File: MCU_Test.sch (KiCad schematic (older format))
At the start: 18 parts, among them U2 STM32F051K6Ux

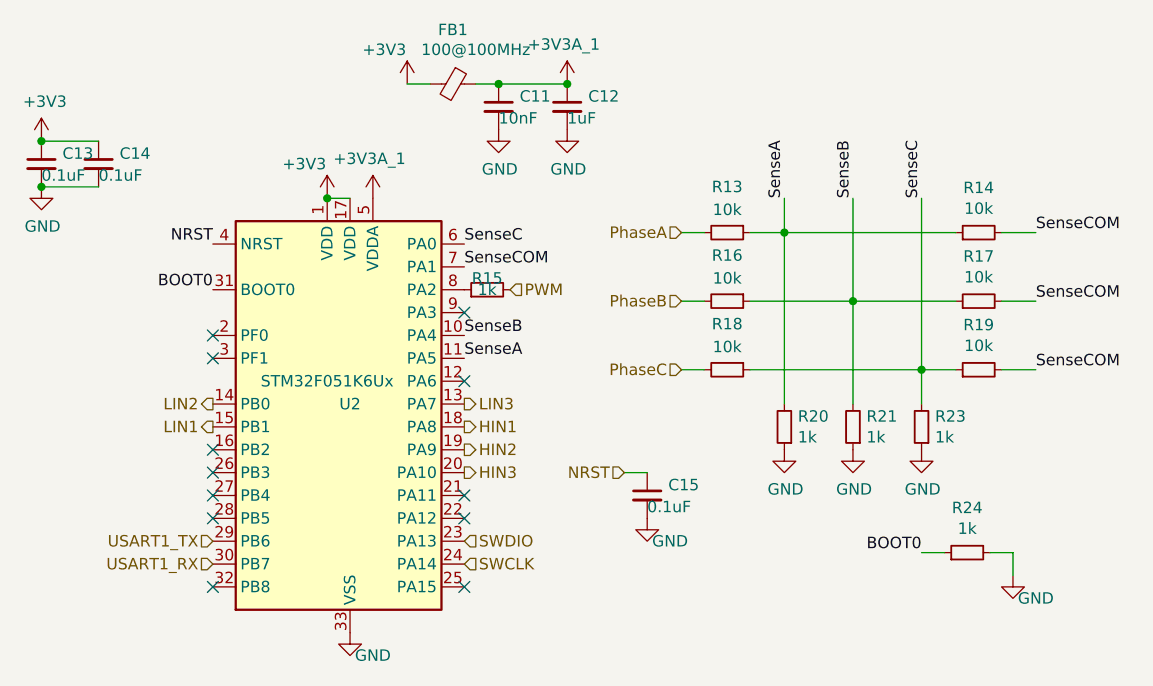
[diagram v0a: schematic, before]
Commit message: Lots of changes made with back being rerouted
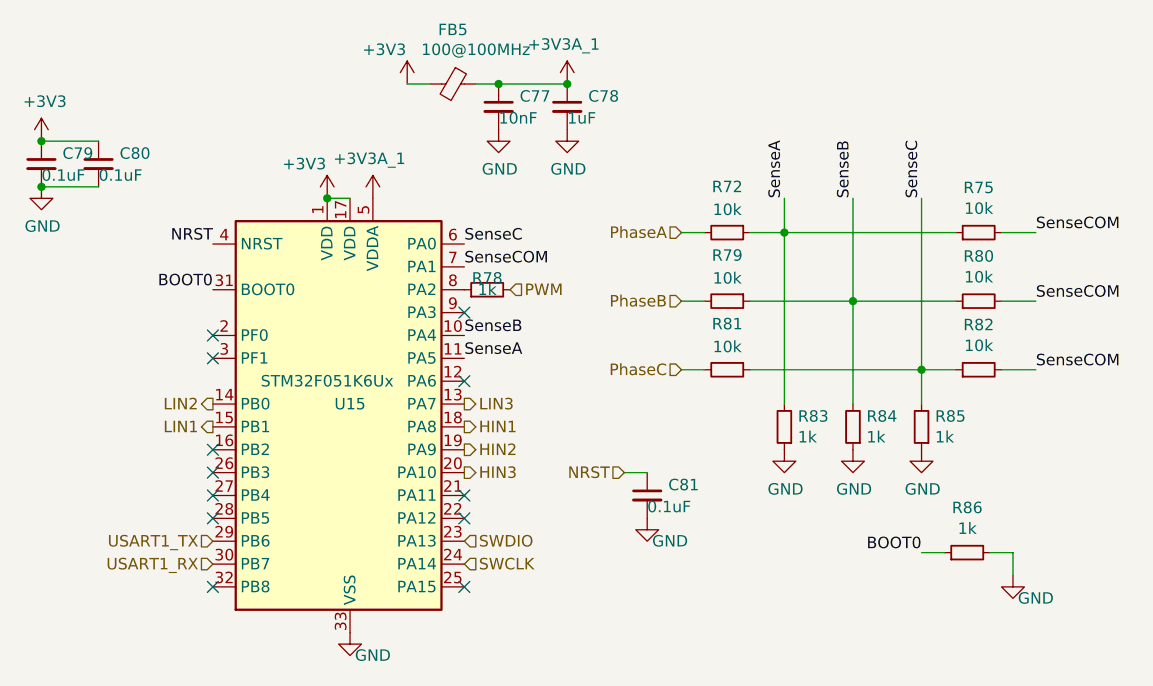
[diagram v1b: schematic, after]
